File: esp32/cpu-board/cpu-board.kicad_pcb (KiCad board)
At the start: 2 copper layers, 99.9 x 69.8 mm, 58 parts, among them J1 Conn_01x07, J2 Conn_01x08, J3 Conn_02x10_Odd_Even, J4 Conn_02x10_Odd_Even, J5 Conn_01x06, J6 Conn_01x07, Q1 PMBTA42DS,125, Q2 PMBTA42DS,125, Q3 PMBTA42DS,125, Q4 PMBTA42DS,125, Q5 PMBTA42DS,125, U1 ESP32-DevBoard2, U2 MAX7320, U3 MAX7320, U4 MAX7320, U5 V7803-1000

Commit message: Finishing touches on the board clean up (until the next round)
[git-p4: depot-paths = "//depot/nixiestat/": change = 330]
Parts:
- moved JP9 5.99 mm to (103.6, 138.0)
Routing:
- net GNDREF: track 477.7 -> 376.9 mm, vias 35 -> 31
- net VCC: track 111.4 -> 63.4 mm, vias 2 -> 1
- net +3.3V: track 280.0 -> 252.0 mm
- net Net-(JP9-Pad2): track 10.4 -> 4.62 mm
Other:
- board text added: "Adr"
- board text added: "^^^Cut if using USB cable"
- board text removed: "Add"
- board text removed: "Cut if using USB cable"

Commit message: Further ground work
[git-p4: depot-paths = "//depot/nixiestat/": change = 332]
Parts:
- moved R7 0.40 mm to (121.9, 137.8)
- moved JP9 0.08 mm to (103.6, 137.9)
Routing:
- net GNDREF: track 376.9 -> 384.1 mm, vias 31 -> 37
- net +3.3V: track 252.0 -> 253.9 mm, vias 14 -> 16
- net I2C_SCL: track 207.8 -> 208.6 mm
- net Net-(C5-Pad1): track 12.4 -> 13.1 mm
- net Net-(C6-Pad1): track 10.5 -> 11.1 mm
- net Net-(JP9-Pad2): track 4.62 -> 4.06 mm

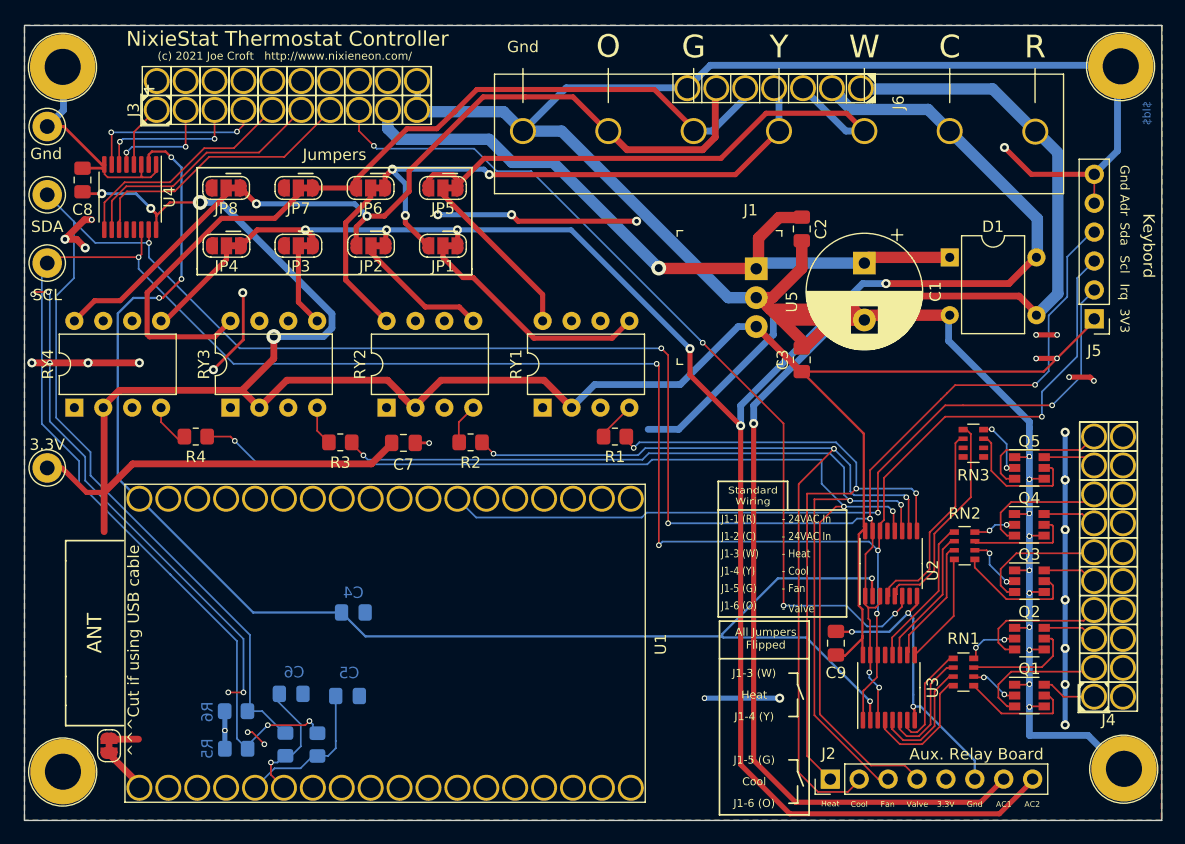
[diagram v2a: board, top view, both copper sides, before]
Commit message: Added RTC
[git-p4: depot-paths = "//depot/nixiestat/": change = 335]
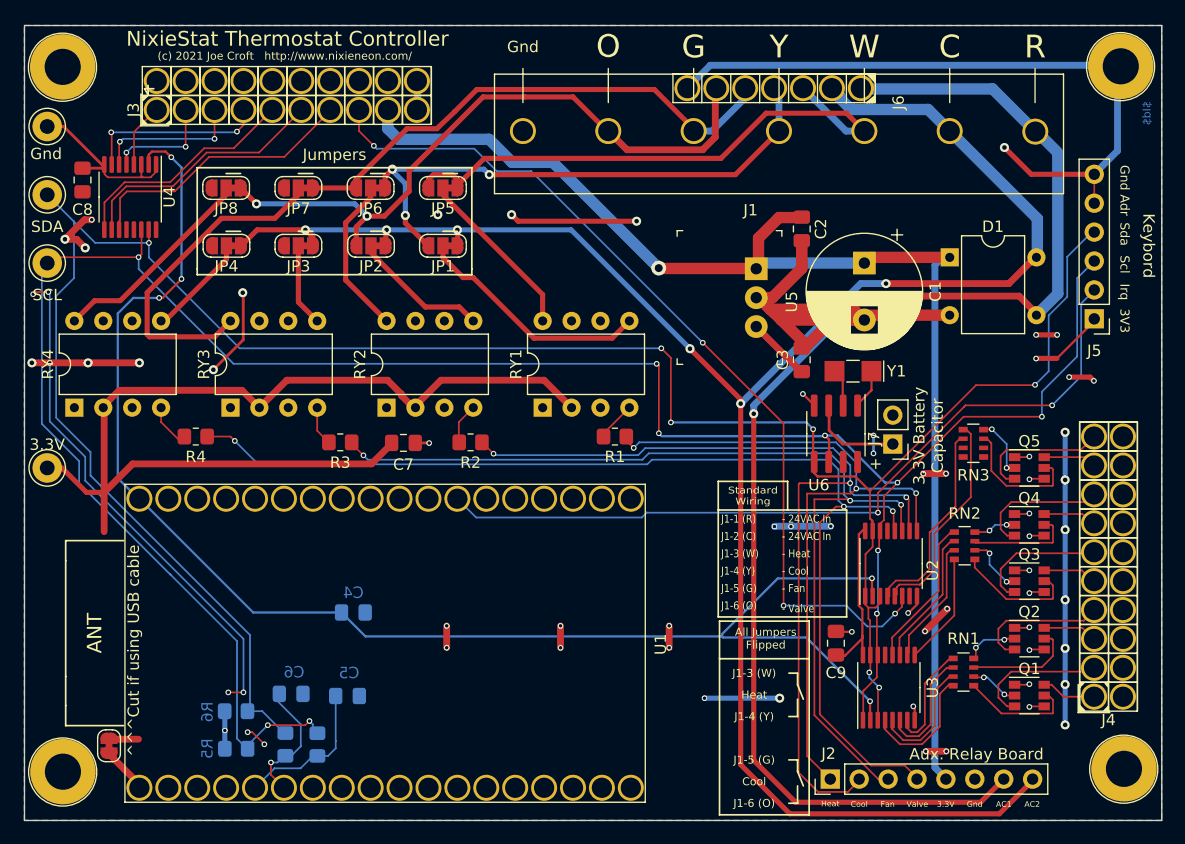
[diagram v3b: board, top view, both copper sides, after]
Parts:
- added J7: Battery, Connector_PinHeader_2.54mm:PinHeader_1x02_P2.54mm_Vertical, F.Cu at (172.5, 111.4)
- added U6: PT7C4339, Package_SO:SOIC-8_3.9x4.9mm_P1.27mm, F.Cu at (167.5, 110.5)
- added Y1: 32.788Khz, Crystal:Crystal_SMD_G8-2Pin_3.2x1.5mm_HandSoldering, F.Cu at (169.0, 105.0)
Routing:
- net GNDREF: track 384.1 -> 242.3 mm, vias 37 -> 50
- net +3.3V: track 253.9 -> 161.1 mm
- net VCC: track 63.4 -> 110.5 mm
- net Net-(J7-Pad1): track 0.00 -> 8.20 mm
- net I2C_SDA: track 208.4 -> 202.5 mm
- net I2C_SCL: track 208.6 -> 203.5 mm, vias 8 -> 10
- net Net-(U6-Pad1): track 0.00 -> 3.41 mm
- net Net-(U6-Pad2): track 0.00 -> 3.10 mm
- net AC2: track 175.2 -> 173.2 mm
- net KEY_IRQ: track 70.8 -> 69.7 mm
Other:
- board text added: "+"
- board text added: "3.3V Battery Capacitor"
